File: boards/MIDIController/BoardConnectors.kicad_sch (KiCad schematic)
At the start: 16 parts, among them J2 MIDICon, J3 IO_Boards

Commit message: Fixed some RX/TX pin swaps
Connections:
- net RXD Panel: now also J3.13 (Pin_13); no longer J3.15 (Pin_15)
- net TXD Panel: now also J3.15 (Pin_15); no longer J3.13 (Pin_13)
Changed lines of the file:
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@@
 	(hierarchical_label "TXD Panel"
 		(shape input)
-		(at 88.9 111.76 180)
+		(at 88.9 114.3 180)
 		(fields_autoplaced yes)
 		(effects
@@
 	(hierarchical_label "RXD Panel"
 		(shape output)
-		(at 88.9 114.3 180)
+		(at 88.9 111.76 180)
 		(fields_autoplaced yes)
 		(effects

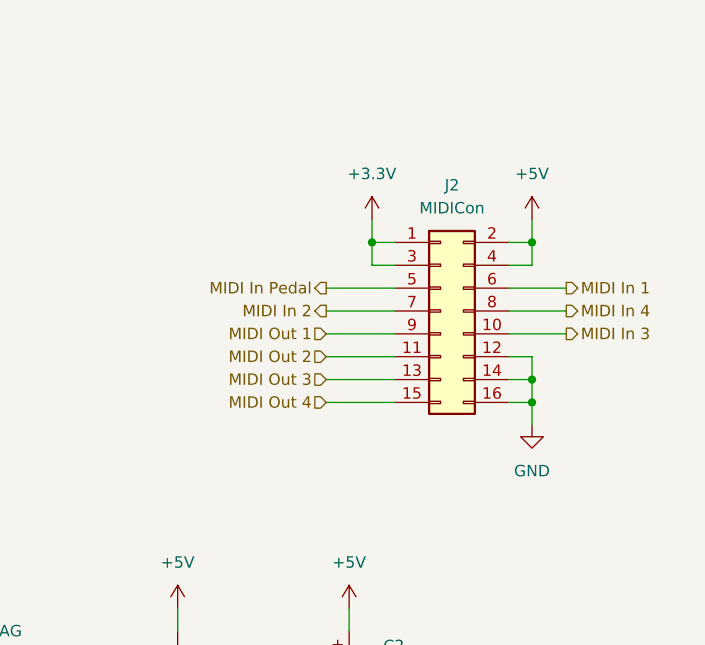
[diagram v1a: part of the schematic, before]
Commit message: Fixed mirrored MIDI board connector
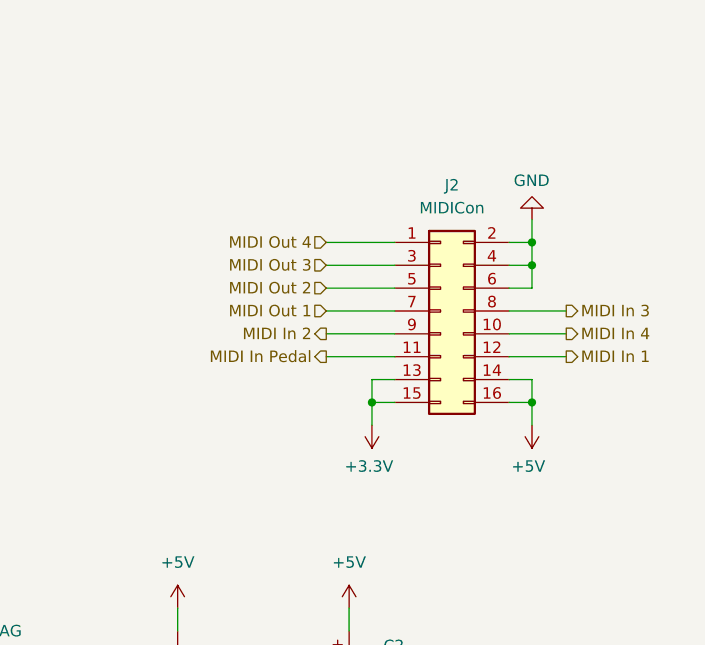
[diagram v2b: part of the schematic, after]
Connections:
- net +3.3V: now also J2.13 (Pin_13), J2.15 (Pin_15); no longer J2.1 (Pin_1), J2.3 (Pin_3)
- net +5V: now also J2.14 (Pin_14), J2.16 (Pin_16); no longer J2.2 (Pin_2), J2.4 (Pin_4)
- net GND: now also J2.2 (Pin_2), J2.4 (Pin_4), J2.6 (Pin_6); no longer J2.12 (Pin_12), J2.14 (Pin_14), J2.16 (Pin_16)
- net MIDI In 1: now also J2.12 (Pin_12); no longer J2.6 (Pin_6)
- net MIDI In 2: now also J2.9 (Pin_9); no longer J2.7 (Pin_7)
- net MIDI In 3: now also J2.8 (Pin_8); no longer J2.10 (Pin_10)
- net MIDI In 4: now also J2.10 (Pin_10); no longer J2.8 (Pin_8)
- net MIDI In Pedal: now also J2.11 (Pin_11); no longer J2.5 (Pin_5)
- net MIDI Out 1: now also J2.7 (Pin_7); no longer J2.9 (Pin_9)
- net MIDI Out 2: now also J2.5 (Pin_5); no longer J2.11 (Pin_11)
- net MIDI Out 3: now also J2.3 (Pin_3); no longer J2.13 (Pin_13)
- net MIDI Out 4: now also J2.1 (Pin_1); no longer J2.15 (Pin_15)
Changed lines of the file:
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@@
+	)
+	(junction
+		(at 168.91 118.11)
+		(diameter 0)
+		(color 0 0 0 0)
 	)
 	(junction
@@
 	)
 	(junction
-		(at 58.42 76.2)
+		(at 186.69 102.87)
 		(diameter 0)
 		(color 0 0 0 0)
 	)
 	(junction
-		(at 186.69 115.57)
+		(at 58.42 76.2)
 		(diameter 0)
 		(color 0 0 0 0)
@@
 	)
 	(junction
-		(at 168.91 100.33)
-		(diameter 0)
-		(color 0 0 0 0)
-	)
-	(junction
 		(at 186.69 100.33)
 		(diameter 0)
@@
 	(wire
 		(pts
-			(xy 168.91 102.87) (xy 171.45 102.87)
+			(xy 163.83 102.87) (xy 171.45 102.87)
 		)
 		(stroke
@@
 	(wire
 		(pts
-			(xy 168.91 100.33) (xy 171.45 100.33)
+			(xy 163.83 100.33) (xy 171.45 100.33)
 		)
 		(stroke
@@
 	(wire
 		(pts
-			(xy 186.69 113.03) (xy 186.69 115.57)
-		)
-		(stroke
-			(width 0)
-			(type default)
-		)
-	)
-	(wire
-		(pts
 			(xy 69.85 43.18) (xy 81.28 43.18)
 		)
@@
 	(wire
 		(pts
-			(xy 184.15 105.41) (xy 190.5 105.41)
-		)
-		(stroke
-			(width 0)
-			(type default)
-		)
-	)
-	(wire
-		(pts
 			(xy 76.2 76.2) (xy 76.2 104.14)
 		)
@@
 	(wire
 		(pts
-			(xy 163.83 118.11) (xy 171.45 118.11)
+			(xy 168.91 115.57) (xy 171.45 115.57)
 		)
 		(stroke
@@
 	(wire
 		(pts
+			(xy 184.15 105.41) (xy 186.69 105.41)
+		)
+		(stroke
+			(width 0)
+			(type default)
+		)
+	)
+	(wire
+		(pts
 			(xy 163.83 105.41) (xy 171.45 105.41)
 		)
@@
 	(wire
 		(pts
+			(xy 168.91 118.11) (xy 171.45 118.11)
+		)
+		(stroke
+			(width 0)
+			(type default)
+		)
+	)
+	(wire
+		(pts
 			(xy 109.22 116.84) (xy 124.46 116.84)
 		)
@@
 	(wire
 		(pts
+			(xy 186.69 105.41) (xy 186.69 102.87)
+		)
+		(stroke
+			(width 0)
+			(type default)
+		)
+	)
+	(wire
+		(pts
 			(xy 184.15 115.57) (xy 186.69 115.57)
 		)
@@
 	(wire
 		(pts
-			(xy 168.91 100.33) (xy 168.91 102.87)
-		)
-		(stroke
-			(width 0)
-			(type default)
-		)
-	)
-	(wire
-		(pts
 			(xy 46.99 109.22) (xy 58.42 109.22)
 		)
@@
 	(wire
 		(pts
-			(xy 163.83 115.57) (xy 171.45 115.57)
-		)
-		(stroke
-			(width 0)
-			(type default)
-		)
-	)
-	(wire
-		(pts
 			(xy 88.9 114.3) (xy 96.52 114.3)
 		)
@@
 	(wire
 		(pts
+			(xy 168.91 120.65) (xy 168.91 118.11)
+		)
+		(stroke
+			(width 0)
+			(type default)
+		)
+	)
+	(wire
+		(pts
 			(xy 109.22 101.6) (xy 113.03 101.6)
 		)
@@
 	(wire
 		(pts
-			(xy 168.91 97.79) (xy 168.91 100.33)
-		)
-		(stroke
-			(width 0)
-			(type default)
-		)
-	)
-	(wire
-		(pts
 			(xy 46.99 92.71) (xy 58.42 92.71)
 		)
@@
 	(wire
 		(pts
-			(xy 184.15 113.03) (xy 186.69 113.03)
+			(xy 184.15 113.03) (xy 190.5 113.03)
 		)
 		(stroke
@@
 		(pts
 			(xy 109.22 109.22) (xy 111.76 109.22)
+		)
+		(stroke
+			(width 0)
+			(type default)
+		)
+	)
+	(wire
+		(pts
+			(xy 168.91 118.11) (xy 168.91 115.57)
 		)
 		(stroke
@@
 	(hierarchical_label "MIDI Out 4"
 		(shape input)
-		(at 163.83 118.11 180)
+		(at 163.83 100.33 180)
 		(fields_autoplaced yes)
 		(effects
@@
 	(hierarchical_label "MIDI Out 1"
 		(shape input)
-		(at 163.83 110.49 180)
+		(at 163.83 107.95 180)
 		(fields_autoplaced yes)
 		(effects
@@
 	(hierarchical_label "MIDI In 4"
 		(shape output)
-		(at 190.5 107.95 0)
+		(at 190.5 110.49 0)
 		(fields_autoplaced yes)
 		(effects
@@
 	(hierarchical_label "MIDI Out 2"
 		(shape input)
-		(at 163.83 113.03 180)
+		(at 163.83 105.41 180)
 		(fields_autoplaced yes)
 		(effects
@@
 	(hierarchical_label "MIDI Out 3"
 		(shape input)
-		(at 163.83 115.57 180)
+		(at 163.83 102.87 180)
 		(fields_autoplaced yes)
 		(effects
@@
 	(hierarchical_label "MIDI In 3"
 		(shape output)
-		(at 190.5 110.49 0)
+		(at 190.5 107.95 0)
 		(fields_autoplaced yes)
 		(effects
@@
 	(hierarchical_label "MIDI In Pedal"
 		(shape output)
-		(at 163.83 105.41 180)
+		(at 163.83 113.03 180)
 		(fields_autoplaced yes)
 		(effects
@@
 	(hierarchical_label "MIDI In 2"
 		(shape output)
-		(at 163.83 107.95 180)
+		(at 163.83 110.49 180)
 		(fields_autoplaced yes)
 		(effects
@@
 	(hierarchical_label "MIDI In 1"
 		(shape output)
-		(at 190.5 105.41 0)
+		(at 190.5 113.03 0)
 		(fields_autoplaced yes)
 		(effects
@@
 	(symbol
 		(lib_id "power:+3.3V")
-		(at 168.91 97.79 0)
+		(at 168.91 120.65 180)
 		(unit 1)
 		(exclude_from_sim no)
@@
 		(on_board yes)
 		(dnp no)
-		(fields_autoplaced yes)
 		(property "Reference" "#PWR03"
-			(at 168.91 101.6 0)
+			(at 168.91 116.84 0)
 			(effects
 				(font
@@
 		)
 		(property "Value" "+3.3V"
-			(at 168.91 92.71 0)
-			(effects
-				(font
-					(size 1.27 1.27)
-				)
+			(at 165.862 125.222 0)
+			(effects
+				(font
+					(size 1.27 1.27)
+				)
+				(justify right)
 			)
 		)
 		(property "Footprint" ""
-			(at 168.91 97.79 0)
+			(at 168.91 120.65 0)
 			(effects
 				(font
@@
 		)
 		(property "Datasheet" ""
-			(at 168.91 97.79 0)
+			(at 168.91 120.65 0)
 			(effects
 				(font
@@
 		)
 		(property "Description" "Power symbol creates a global label with name \"+3.3V\""
-			(at 168.91 97.79 0)
+			(at 168.91 120.65 0)
 			(effects
 				(font
@@
 	(symbol
 		(lib_id "power:GND")
-		(at 186.69 120.65 0)
+		(at 186.69 97.79 180)
 		(unit 1)
 		(exclude_from_sim no)
@@
 		(on_board yes)
 		(dnp no)
-		(fields_autoplaced yes)
 		(property "Reference" "#PWR02"
-			(at 186.69 127 0)
+			(at 186.69 91.44 0)
 			(effects
 				(font
@@
 		)
 		(property "Value" "GND"
-			(at 186.69 125.73 0)
-			(effects
-				(font
-					(size 1.27 1.27)
-				)
+			(at 184.658 93.472 0)
+			(effects
+				(font
+					(size 1.27 1.27)
+				)
+				(justify right)
 			)
 		)
 		(property "Footprint" ""
-			(at 186.69 120.65 0)
+			(at 186.69 97.79 0)
 			(effects
 				(font
@@
 		)
 		(property "Datasheet" ""
-			(at 186.69 120.65 0)
+			(at 186.69 97.79 0)
 			(effects
 				(font
@@
 		)
 		(property "Description" "Power symbol creates a global label with name \"GND\" , ground"
-			(at 186.69 120.65 0)
+			(at 186.69 97.79 0)
 			(effects
 				(font
@@
 	(symbol
 		(lib_id "power:+5V")
-		(at 186.69 97.79 0)
+		(at 186.69 120.65 180)
 		(unit 1)
 		(exclude_from_sim no)
@@
 		(on_board yes)
 		(dnp no)
-		(fields_autoplaced yes)
 		(property "Reference" "#PWR01"
-			(at 186.69 101.6 0)
+			(at 186.69 116.84 0)
 			(effects
 				(font
@@
 		)
 		(property "Value" "+5V"
-			(at 186.69 92.71 0)
-			(effects
-				(font
-					(size 1.27 1.27)
-				)
+			(at 184.404 125.222 0)
+			(effects
+				(font
+					(size 1.27 1.27)
+				)
+				(justify right)
 			)
 		)
 		(property "Footprint" ""
-			(at 186.69 97.79 0)
+			(at 186.69 120.65 0)
 			(effects
 				(font
@@
 		)
 		(property "Datasheet" ""
-			(at 186.69 97.79 0)
+			(at 186.69 120.65 0)
 			(effects
 				(font
@@
 		)
 		(property "Description" "Power symbol creates a global label with name \"+5V\""
-			(at 186.69 97.79 0)
-			(effects
-				(font
+			(at 186.69 120.65 0)
+			(effects
+				(font

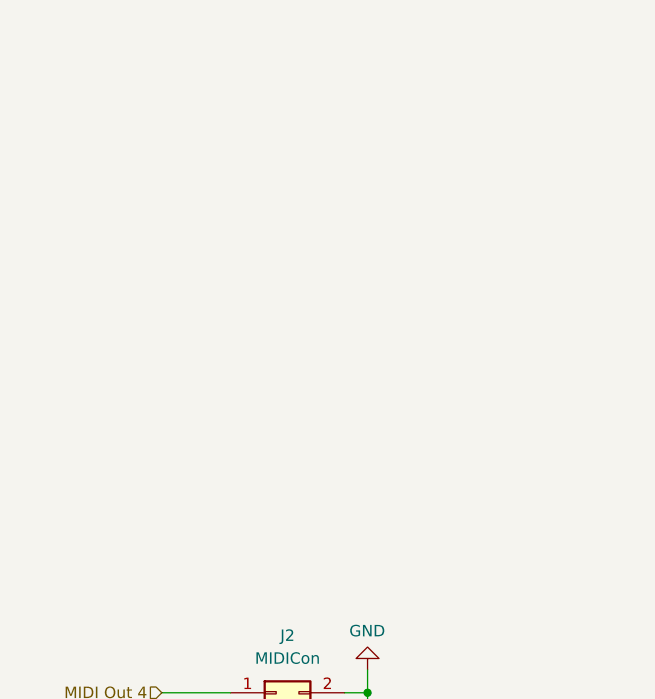
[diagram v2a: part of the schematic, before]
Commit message: Added line jacks for the audio board.
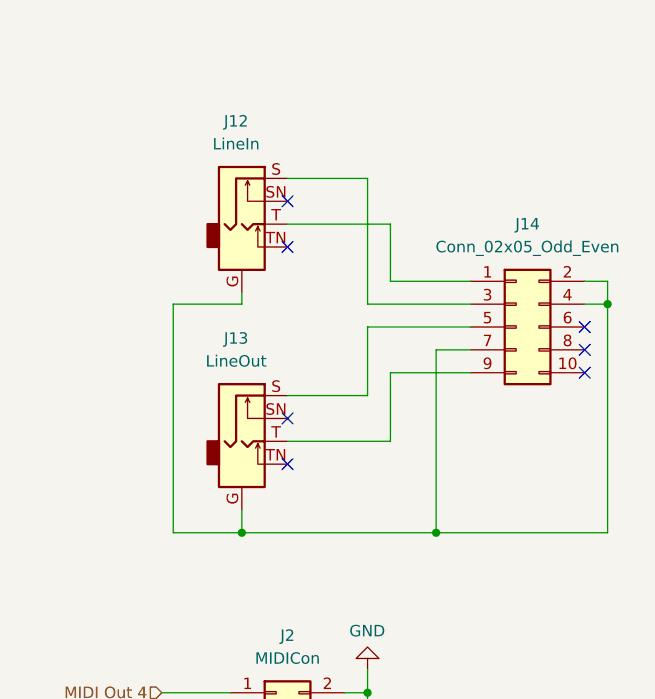
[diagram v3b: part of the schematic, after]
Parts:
- added J12: LineIn, Custom_Connectors:Jack_3.5mm_Ledino_KB3SPRS_Horizontal_Stereo, symbol Connector_Audio:AudioJack2_Ground_Switch
- added J13: LineOut, Custom_Connectors:Jack_3.5mm_Ledino_KB3SPRS_Horizontal_Stereo, symbol Connector_Audio:AudioJack2_Ground_Switch
- added J14: Conn_02x05_Odd_Even, Connector_PinHeader_2.54mm:PinHeader_2x05_P2.54mm_Vertical, symbol Connector_Generic:Conn_02x05_Odd_Even
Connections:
- new net: J12.G, J13.G, J14.2 (Pin_2), J14.4 (Pin_4), J14.7 (Pin_7)
- new net: J12.S, J14.3 (Pin_3)
- new net: J12.T, J14.1 (Pin_1)
- new net: J13.S, J14.5 (Pin_5)
- new net: J13.T, J14.9 (Pin_9)
- no-connect marks 0 -> 7
